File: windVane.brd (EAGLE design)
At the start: 25 x 25 mm, 10 parts, among them IC1 S-5712ANDL2-I4T1U, IC2 S-5712ANDL2-I4T1U, IC3 S-5712ANDL2-I4T1U, IC4 S-5712ANDL2-I4T1U

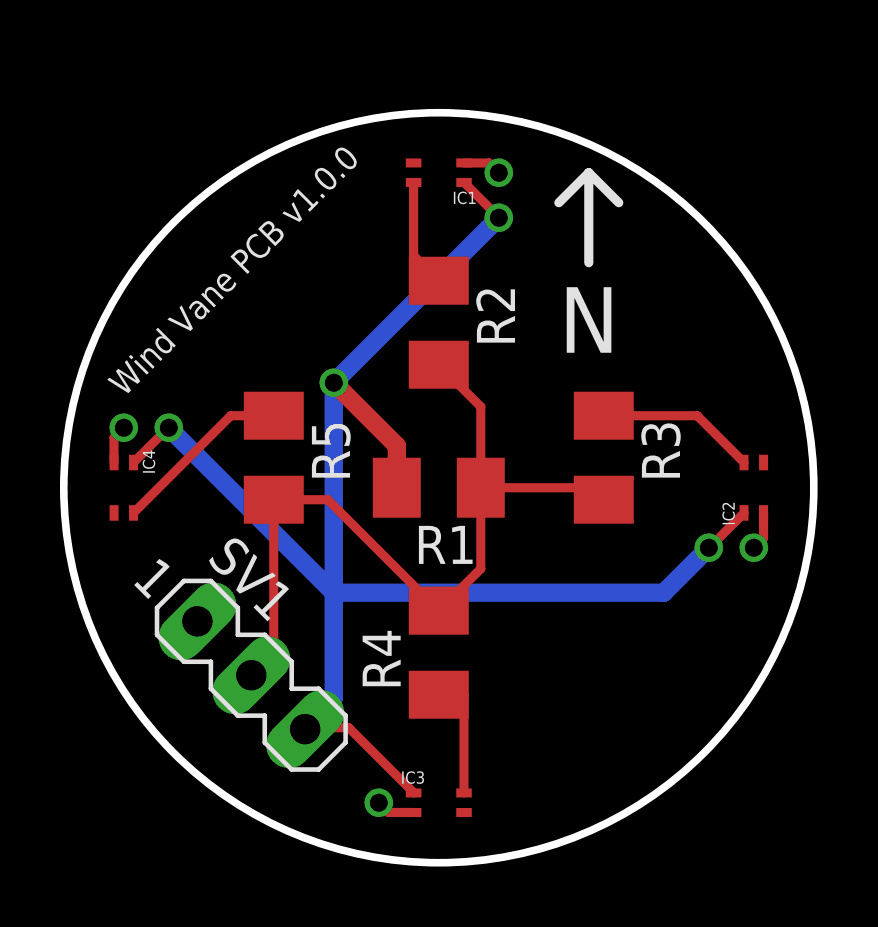
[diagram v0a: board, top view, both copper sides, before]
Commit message: Change placement of header pin for communication board, and changed to vector text in windVane layout
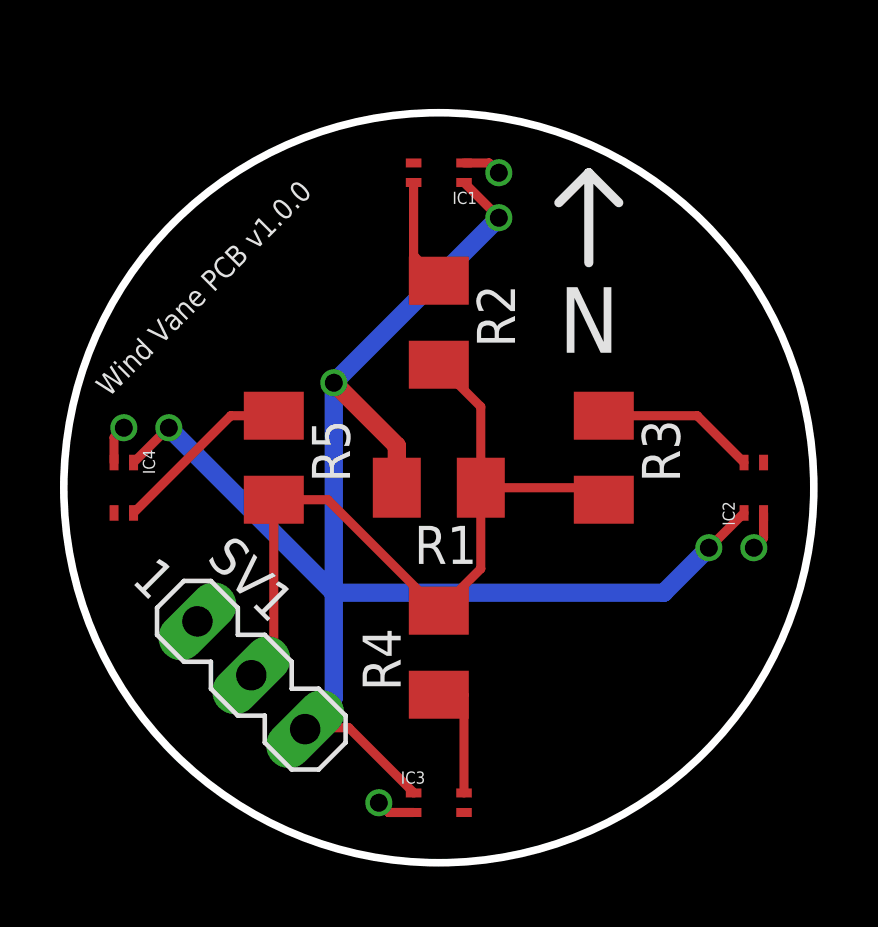
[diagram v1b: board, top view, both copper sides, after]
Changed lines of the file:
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@@
 <wire x1="16.5" y1="22" x2="17.5" y2="23" width="0.3048" layer="21"/>
 <wire x1="17.5" y1="23" x2="18.5" y2="22" width="0.3048" layer="21"/>
-<text x="2" y="15.5" size="0.8128" layer="21" rot="R45">Wind Vane PCB v1.0.0</text>
+<text x="1.5" y="15.5" size="0.7" layer="21" font="vector" ratio="15" rot="R45">Wind Vane PCB v1.0.0</text>
 </plain>
 <attributes>
@@
 </class>
 </classes>
-<designrules name="LaenPCBOrder">
-<description language="de">&lt;b&gt;EAGLE Design Rules&lt;/b&gt;
-&lt;p&gt;
-Die Standard-Design-Rules sind so gewählt, dass sie für
-die meisten Anwendungen passen. Sollte ihre Platine
-besondere Anforderungen haben, treffen Sie die erforderlichen
-Einstellungen hier und speichern die Design Rules unter
-einem neuen Namen ab.</description>
-<description language="en">&lt;b&gt;Laen's PCB Order Design Rules&lt;/b&gt;
-&lt;p&gt;
-Please make sure your boards conform to these design rules.</description>
+<designrules name="dirt_cheap_dirty_boards.v1">
+<description language="en">&lt;b&gt;Dirty Cheap Dirty Board Design Rules&lt;/b&gt;
+&lt;br&gt;
+&lt;br&gt;Min width/Spacing: 5/5mil
+&lt;br&gt;Min diameter of finished hole 12mil</description>
 <param name="layerSetup" value="(1*16)"/>
-<param name="mtCopper" value="0.0356mm 0.0356mm 0.0356mm 0.0356mm 0.0356mm 0.0356mm 0.0356mm 0.0356mm 0.0356mm 0.0356mm 0.0356mm 0.0356mm 0.0356mm 0.0356mm 0.0356mm 0.0356mm"/>
-<param name="mtIsolate" value="1.5011mm 0.1499mm 0.2007mm 0.1499mm 0.2007mm 0.1499mm 0.2007mm 0.1499mm 0.2007mm 0.1499mm 0.2007mm 0.1499mm 0.2007mm 0.1499mm 0.2007mm"/>
-<param name="mdWireWire" value="6mil"/>
-<param name="mdWirePad" value="6mil"/>
-<param name="mdWireVia" value="6mil"/>
-<param name="mdPadPad" value="6mil"/>
-<param name="mdPadVia" value="6mil"/>
-<param name="mdViaVia" value="6mil"/>
-<param name="mdSmdPad" value="6mil"/>
-<param name="mdSmdVia" value="6mil"/>
-<param name="mdSmdSmd" value="6mil"/>
+<param name="mtCopper" value="0.035mm 0.0175mm 0.035mm 0.035mm 0.035mm 0.035mm 0.035mm 0.035mm 0.035mm 0.035mm 0.035mm 0.035mm 0.035mm 0.035mm 0.0175mm 0.035mm"/>
+<param name="mtIsolate" value="1.5mm 1.1mm 0.2mm 0.15mm 0.2mm 0.15mm 0.2mm 0.15mm 0.2mm 0.15mm 0.2mm 0.15mm 0.2mm 0.15mm 0.2mm"/>
+<param name="mdWireWire" value="5mil"/>
+<param name="mdWirePad" value="5mil"/>
+<param name="mdWireVia" value="5mil"/>
+<param name="mdPadPad" value="5mil"/>
+<param name="mdPadVia" value="5mil"/>
+<param name="mdViaVia" value="5mil"/>
+<param name="mdSmdPad" value="0mil"/>
+<param name="mdSmdVia" value="0mil"/>
+<param name="mdSmdSmd" value="0mil"/>
 <param name="mdViaViaSameLayer" value="8mil"/>
 <param name="mnLayersViaInSmd" value="2"/>
-<param name="mdCopperDimension" value="15mil"/>
-<param name="mdDrill" value="6mil"/>
+<param name="mdCopperDimension" value="10mil"/>
+<param name="mdDrill" value="10mil"/>
 <param name="mdSmdStop" value="0mil"/>
-<param name="msWidth" value="6mil"/>
-<param name="msDrill" value="13mil"/>
-<param name="msMicroVia" value="13mil"/>
+<param name="msWidth" value="5mil"/>
+<param name="msDrill" value="12mil"/>
+<param name="msMicroVia" value="12mil"/>
 <param name="msBlindViaRatio" value="0.5"/>
 <param name="rvPadTop" value="0.25"/>
@@
 <param name="rvMicroViaOuter" value="0.25"/>
 <param name="rvMicroViaInner" value="0.25"/>
-<param name="rlMinPadTop" value="7mil"/>
+<param name="rlMinPadTop" value="10mil"/>
 <param name="rlMaxPadTop" value="20mil"/>
-<param name="rlMinPadInner" value="7mil"/>
+<param name="rlMinPadInner" value="10mil"/>
 <param name="rlMaxPadInner" value="20mil"/>
-<param name="rlMinPadBottom" value="7mil"/>
+<param name="rlMinPadBottom" value="10mil"/>
 <param name="rlMaxPadBottom" value="20mil"/>
-<param name="rlMinViaOuter" value="7mil"/>
+<param name="rlMinViaOuter" value="6mil"/>
 <param name="rlMaxViaOuter" value="20mil"/>
-<param name="rlMinViaInner" value="7mil"/>
+<param name="rlMinViaInner" value="6mil"/>
 <param name="rlMaxViaInner" value="20mil"/>
 <param name="rlMinMicroViaOuter" value="4mil"/>
@@
 <param name="psTop" value="-1"/>
 <param name="psBottom" value="-1"/>
-<param name="psFirst" value="-1"/>
+<param name="psFirst" value="0"/>
 <param name="psElongationLong" value="100"/>
 <param name="psElongationOffset" value="100"/>
 <param name="mvStopFrame" value="1"/>
 <param name="mvCreamFrame" value="0"/>
-<param name="mlMinStopFrame" value="3mil"/>
-<param name="mlMaxStopFrame" value="3mil"/>
+<param name="mlMinStopFrame" value="2mil"/>
+<param name="mlMaxStopFrame" value="2mil"/>
 <param name="mlMinCreamFrame" value="0mil"/>
 <param name="mlMaxCreamFrame" value="0mil"/>
-<param name="mlViaStopLimit" value="0mil"/>
+<param name="mlViaStopLimit" value="25mil"/>
 <param name="srRoundness" value="0"/>
 <param name="srMinRoundness" value="0mil"/>
@@
 <param name="checkAngle" value="0"/>
 <param name="checkFont" value="1"/>
-<param name="checkRestrict" value="1"/>
+<param name="checkRestrict" value="0"/>
 <param name="useDiameter" value="13"/>
 <param name="maxErrors" value="50"/>
